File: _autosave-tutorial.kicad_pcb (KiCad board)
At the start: 2 copper layers, 174.4 x 164.8 mm, 64 parts

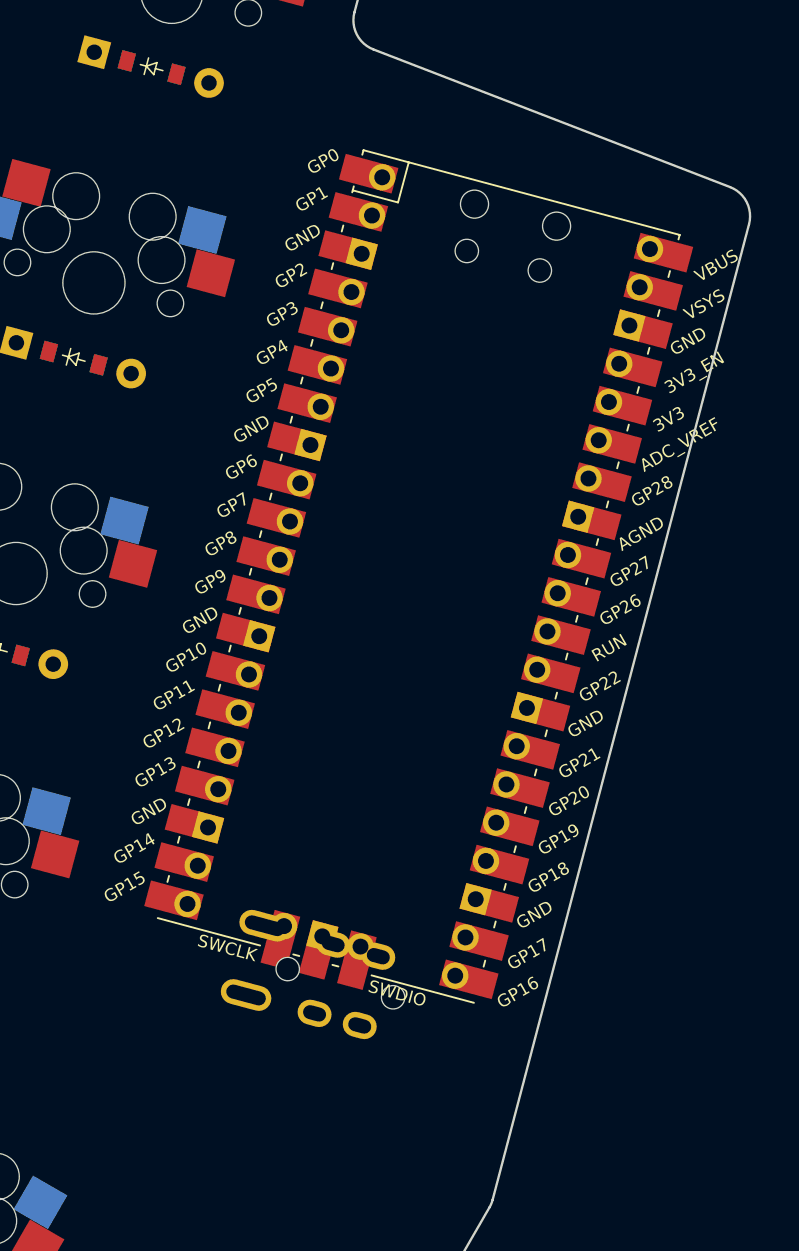
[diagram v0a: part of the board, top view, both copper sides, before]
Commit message: added pico, moved parts around
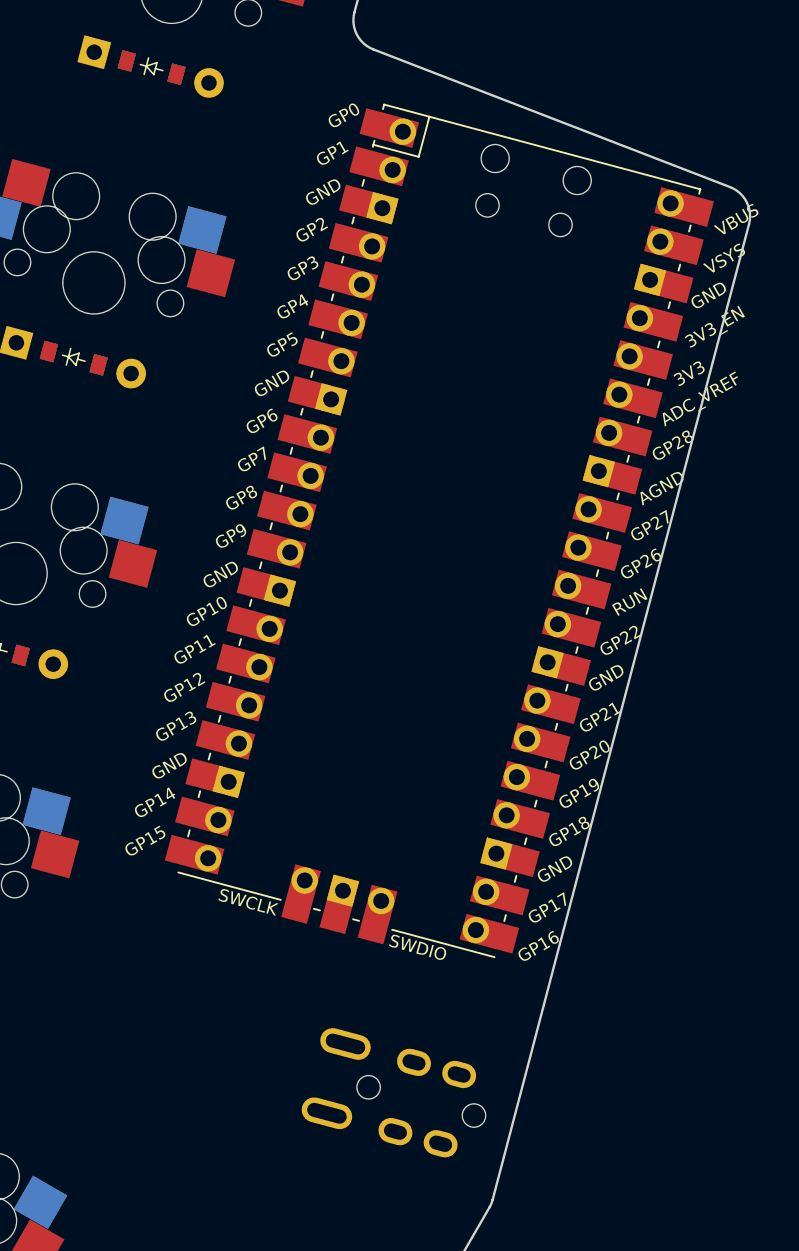
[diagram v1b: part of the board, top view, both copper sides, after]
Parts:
- moved TRRS1 9.19 mm to (214.5, 130.5)
- moved _1 3.21 mm to (210.7, 92.6)
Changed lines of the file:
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@@
 	(footprint "RPi_Pico_SMD_TH"
 		(layer "F.Cu")
-		(at 209.404157 95.553697 -15)
+		(at 210.730194 92.627828 -15)
 		(property "Reference" "_1"
 			(at 0 0 0)
@@
 			)
 		)
-		(fp_text user "Copper Keepouts shown on Dwgs layer"
-			(at 0.1 -30.2 0)
-			(layer "Cmts.User")
-			(effects
-				(font
-					(size 1 1)
-					(thickness 0.15)
-				)
-			)
-		)
 		(fp_text user "${REFERENCE}"
 			(at 0 0 180)
@@
 	(footprint "ceoloide:trrs_pj320a (reversible, symmetric)"
 		(layer "F.Cu")
-		(at 209.306933 122.962465 -105)
+		(at 214.495679 130.54985 -105)
 		(property "Reference" "TRRS1"
 			(at 0 14.2 -105)
